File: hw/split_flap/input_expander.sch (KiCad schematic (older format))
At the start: 17 parts, among them J1 Conn_01x02, J2 Conn_01x02, J3 Conn_01x02, J4 Conn_01x02, J5 Conn_01x02, J6 Conn_01x02, J7 Conn_01x02, J8 Conn_01x02, U4 PCF8574

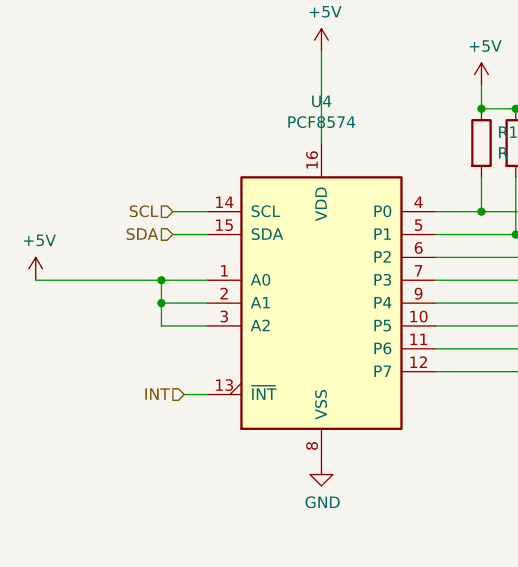
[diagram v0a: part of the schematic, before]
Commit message: Rework PCB
Start routing all expanders
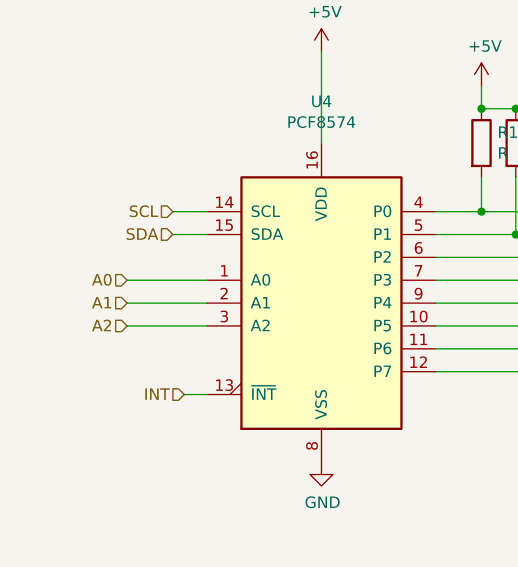
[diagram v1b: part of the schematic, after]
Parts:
- R1, R2, R3, R4, R5, R6, R7, R8: footprint Resistor_THT:R_Axial_DIN0207_L6.3mm_D2.5mm_P10.16mm_Horizontal -> Resistor_SMD:R_0805_2012Metric_Pad1.15x1.40mm_HandSolder
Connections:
- net +5V: no longer U4.1 (A0), U4.2 (A1), U4.3 (A2)
- new net A0: U4.1 (A0)
- new net A1: U4.2 (A1)
- new net A2: U4.3 (A2)
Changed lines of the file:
@@
 $Descr A4 11693 8268
 encoding utf-8
-Sheet 4 6
+Sheet 3 6
 Title ""
 Date ""
@@
 	4700 3100 4700 2700
 Wire Wire Line
-	4000 3700 4000 3800
-Wire Wire Line
-	4000 3700 4200 3700
-Wire Wire Line
-	4000 3800 4200 3800
-Wire Wire Line
 	4050 3400 4200 3400
 Wire Wire Line
 	4200 3500 4050 3500
-Wire Wire Line
-	4200 3900 4000 3900
 $Comp
 L power:GND #PWR?
@@
 F 0 "R2" H 5620 3146 50  0000 L CNN
 F 1 "R" H 5620 3055 50  0000 L CNN
-F 2 "Resistor_THT:R_Axial_DIN0207_L6.3mm_D2.5mm_P10.16mm_Horizontal" V 5480 3100 50  0001 C CNN
+F 2 "Resistor_SMD:R_0805_2012Metric_Pad1.15x1.40mm_HandSolder" V 5480 3100 50  0001 C CNN
 F 3 "~" H 5550 3100 50  0001 C CNN
 	1    5550 3100
@@
 F 0 "R3" H 5770 3146 50  0000 L CNN
 F 1 "R" H 5770 3055 50  0000 L CNN
-F 2 "Resistor_THT:R_Axial_DIN0207_L6.3mm_D2.5mm_P10.16mm_Horizontal" V 5630 3100 50  0001 C CNN
+F 2 "Resistor_SMD:R_0805_2012Metric_Pad1.15x1.40mm_HandSolder" V 5630 3100 50  0001 C CNN
 F 3 "~" H 5700 3100 50  0001 C CNN
 	1    5700 3100
@@
 F 0 "R4" H 5920 3146 50  0000 L CNN
 F 1 "R" H 5920 3055 50  0000 L CNN
-F 2 "Resistor_THT:R_Axial_DIN0207_L6.3mm_D2.5mm_P10.16mm_Horizontal" V 5780 3100 50  0001 C CNN
+F 2 "Resistor_SMD:R_0805_2012Metric_Pad1.15x1.40mm_HandSolder" V 5780 3100 50  0001 C CNN
 F 3 "~" H 5850 3100 50  0001 C CNN
 	1    5850 3100
@@
 F 0 "R5" H 6070 3146 50  0000 L CNN
 F 1 "R" H 6070 3055 50  0000 L CNN
-F 2 "Resistor_THT:R_Axial_DIN0207_L6.3mm_D2.5mm_P10.16mm_Horizontal" V 5930 3100 50  0001 C CNN
+F 2 "Resistor_SMD:R_0805_2012Metric_Pad1.15x1.40mm_HandSolder" V 5930 3100 50  0001 C CNN
 F 3 "~" H 6000 3100 50  0001 C CNN
 	1    6000 3100
@@
 F 0 "R6" H 6220 3146 50  0000 L CNN
 F 1 "R" H 6220 3055 50  0000 L CNN
-F 2 "Resistor_THT:R_Axial_DIN0207_L6.3mm_D2.5mm_P10.16mm_Horizontal" V 6080 3100 50  0001 C CNN
+F 2 "Resistor_SMD:R_0805_2012Metric_Pad1.15x1.40mm_HandSolder" V 6080 3100 50  0001 C CNN
 F 3 "~" H 6150 3100 50  0001 C CNN
 	1    6150 3100
@@
 F 0 "R7" H 6370 3146 50  0000 L CNN
 F 1 "R" H 6370 3055 50  0000 L CNN
-F 2 "Resistor_THT:R_Axial_DIN0207_L6.3mm_D2.5mm_P10.16mm_Horizontal" V 6230 3100 50  0001 C CNN
+F 2 "Resistor_SMD:R_0805_2012Metric_Pad1.15x1.40mm_HandSolder" V 6230 3100 50  0001 C CNN
 F 3 "~" H 6300 3100 50  0001 C CNN
 	1    6300 3100
@@
 F 0 "R1" H 5470 3146 50  0000 L CNN
 F 1 "R" H 5470 3055 50  0000 L CNN
-F 2 "Resistor_THT:R_Axial_DIN0207_L6.3mm_D2.5mm_P10.16mm_Horizontal" V 5330 3100 50  0001 C CNN
+F 2 "Resistor_SMD:R_0805_2012Metric_Pad1.15x1.40mm_HandSolder" V 5330 3100 50  0001 C CNN
 F 3 "~" H 5400 3100 50  0001 C CNN
 	1    5400 3100
@@
 F 0 "R8" H 6520 3146 50  0000 L CNN
 F 1 "R" H 6520 3055 50  0000 L CNN
-F 2 "Resistor_THT:R_Axial_DIN0207_L6.3mm_D2.5mm_P10.16mm_Horizontal" V 6380 3100 50  0001 C CNN
+F 2 "Resistor_SMD:R_0805_2012Metric_Pad1.15x1.40mm_HandSolder" V 6380 3100 50  0001 C CNN
 F 3 "~" H 6450 3100 50  0001 C CNN
 	1    6450 3100
@@
 	6450 4100 6750 4100
 Wire Wire Line
-	4000 3800 4000 3900
-Connection ~ 4000 3800
-Connection ~ 4000 3700
-Wire Wire Line
 	4100 4200 4200 4200
-$Comp
-L power:+5V #PWR?
-U 1 1 5E06FDAF
-P 3450 3700
-AR Path="/5E06FDAF" Ref="#PWR?"  Part="1"
-AR Path="/5E065378/5E06FDAF" Ref="#PWR014"  Part="1"
-F 0 "#PWR014" H 3450 3550 50  0001 C CNN
-F 1 "+5V" H 3465 3873 50  0000 C CNN
-F 2 "" H 3450 3700 50  0001 C CNN
-F 3 "" H 3450 3700 50  0001 C CNN
-	1    3450 3700
-	1    0    0    -1
-$EndComp
 $Comp
 L power:+5V #PWR?
@@
 Text HLabel 4050 3400 0    50   Input ~ 0
 SCL
-Wire Wire Line
-	3450 3700 4000 3700
 Text HLabel 4050 3500 0    50   Input ~ 0
 SDA
 Text HLabel 4100 4200 0    50   Input ~ 0
 INT
+Text HLabel 3850 3700 0    50   Input ~ 0
+A0
+Text HLabel 3850 3800 0    50   Input ~ 0
+A1
+Text HLabel 3850 3900 0    50   Input ~ 0
+A2
+Wire Wire Line
+	3850 3900 4200 3900
+Wire Wire Line
+	3850 3800 4200 3800
+Wire Wire Line
+	3850 3700 4200 3700
 $EndSCHEMATC

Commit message: Add VCC for motors
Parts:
- J1, J2, J3, J4, J5, J6, J7, J8: footprint Connector_JST:JST_XH_B2B-XH-A_1x02_P2.50mm_Vertical -> Connector_JST:JST_XH_B3B-XH-A_1x03_P2.50mm_Vertical; symbol Connector_Generic:Conn_01x02 -> Connector_Generic:Conn_01x03
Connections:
- net +5V: now also J1.2 (Pin_2), J2.2 (Pin_2), J3.2 (Pin_2), J4.2 (Pin_2), J5.2 (Pin_2), J6.2 (Pin_2), J7.2 (Pin_2), J8.2 (Pin_2)
- net GND: now also J1.3 (Pin_3), J2.3 (Pin_3), J3.3 (Pin_3), J4.3 (Pin_3), J5.3 (Pin_3), J6.3 (Pin_3), J7.3 (Pin_3), J8.3 (Pin_3); no longer J1.2 (Pin_2), J2.2 (Pin_2), J3.2 (Pin_2), J4.2 (Pin_2), J5.2 (Pin_2), J6.2 (Pin_2), J7.2 (Pin_2), J8.2 (Pin_2)
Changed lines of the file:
@@
 $EndComp
-Wire Wire Line
-	6750 4950 7050 4950
-Wire Wire Line
-	6750 4100 6750 4950
 Wire Wire Line
 	5200 4100 6450 4100
-Wire Wire Line
-	6800 4550 7050 4550
-Wire Wire Line
-	6800 4000 6800 4550
-Wire Wire Line
-	6850 4150 7050 4150
-Wire Wire Line
-	6850 3900 6850 4150
-Wire Wire Line
-	6900 3750 7050 3750
-Wire Wire Line
-	6900 3800 6900 3750
-Wire Wire Line
-	6850 3350 7050 3350
-Wire Wire Line
-	6850 3700 6850 3350
-Wire Wire Line
-	6800 2950 7050 2950
-Wire Wire Line
-	6800 3600 6800 2950
-Wire Wire Line
-	6750 2550 7050 2550
-Wire Wire Line
-	6750 3500 6750 2550
-Wire Wire Line
-	6700 2150 7050 2150
-Wire Wire Line
-	6700 3400 6700 2150
 $Comp
 L power:GND #PWR?
@@
 $EndComp
 $Comp
-L Connector_Generic:Conn_01x02 J?
-U 1 1 5E06FCF0
-P 7250 2150
-AR Path="/5E06FCF0" Ref="J?"  Part="1"
-AR Path="/5E065378/5E06FCF0" Ref="J1"  Part="1"
-F 0 "J1" H 7330 2142 50  0000 L CNN
-F 1 "Conn_01x02" H 7330 2051 50  0000 L CNN
-F 2 "Connector_JST:JST_XH_B2B-XH-A_1x02_P2.50mm_Vertical" H 7250 2150 50  0001 C CNN
-F 3 "~" H 7250 2150 50  0001 C CNN
-	1    7250 2150
-	1    0    0    -1
-$EndComp
-$Comp
 L power:GND #PWR?
 U 1 1 5E06FCF6
@@
 $EndComp
 $Comp
-L Connector_Generic:Conn_01x02 J?
+L Connector_Generic:Conn_01x03 J?
 U 1 1 5E06FCFC
 P 7250 2550
@@
 F 0 "J2" H 7330 2542 50  0000 L CNN
 F 1 "Conn_01x02" H 7330 2451 50  0000 L CNN
-F 2 "Connector_JST:JST_XH_B2B-XH-A_1x02_P2.50mm_Vertical" H 7250 2550 50  0001 C CNN
+F 2 "Connector_JST:JST_XH_B3B-XH-A_1x03_P2.50mm_Vertical" H 7250 2550 50  0001 C CNN
 F 3 "~" H 7250 2550 50  0001 C CNN
 	1    7250 2550
@@
 $EndComp
 $Comp
-L Connector_Generic:Conn_01x02 J?
+L Connector_Generic:Conn_01x03 J?
 U 1 1 5E06FD08
 P 7250 2950
@@
 F 0 "J3" H 7330 2942 50  0000 L CNN
 F 1 "Conn_01x02" H 7330 2851 50  0000 L CNN
-F 2 "Connector_JST:JST_XH_B2B-XH-A_1x02_P2.50mm_Vertical" H 7250 2950 50  0001 C CNN
+F 2 "Connector_JST:JST_XH_B3B-XH-A_1x03_P2.50mm_Vertical" H 7250 2950 50  0001 C CNN
 F 3 "~" H 7250 2950 50  0001 C CNN
 	1    7250 2950
@@
 $EndComp
 $Comp
-L Connector_Generic:Conn_01x02 J?
+L Connector_Generic:Conn_01x03 J?
 U 1 1 5E06FD14
 P 7250 3350
@@
 F 0 "J4" H 7330 3342 50  0000 L CNN
 F 1 "Conn_01x02" H 7330 3251 50  0000 L CNN
-F 2 "Connector_JST:JST_XH_B2B-XH-A_1x02_P2.50mm_Vertical" H 7250 3350 50  0001 C CNN
+F 2 "Connector_JST:JST_XH_B3B-XH-A_1x03_P2.50mm_Vertical" H 7250 3350 50  0001 C CNN
 F 3 "~" H 7250 3350 50  0001 C CNN
 	1    7250 3350
@@
 $EndComp
 $Comp
-L Connector_Generic:Conn_01x02 J?
+L Connector_Generic:Conn_01x03 J?
 U 1 1 5E06FD20
 P 7250 3750
@@
 F 0 "J5" H 7330 3742 50  0000 L CNN
 F 1 "Conn_01x02" H 7330 3651 50  0000 L CNN
-F 2 "Connector_JST:JST_XH_B2B-XH-A_1x02_P2.50mm_Vertical" H 7250 3750 50  0001 C CNN
+F 2 "Connector_JST:JST_XH_B3B-XH-A_1x03_P2.50mm_Vertical" H 7250 3750 50  0001 C CNN
 F 3 "~" H 7250 3750 50  0001 C CNN
 	1    7250 3750
@@
 $EndComp
 $Comp
-L Connector_Generic:Conn_01x02 J?
+L Connector_Generic:Conn_01x03 J?
 U 1 1 5E06FD2C
 P 7250 4150
@@
 F 0 "J6" H 7330 4142 50  0000 L CNN
 F 1 "Conn_01x02" H 7330 4051 50  0000 L CNN
-F 2 "Connector_JST:JST_XH_B2B-XH-A_1x02_P2.50mm_Vertical" H 7250 4150 50  0001 C CNN
+F 2 "Connector_JST:JST_XH_B3B-XH-A_1x03_P2.50mm_Vertical" H 7250 4150 50  0001 C CNN
 F 3 "~" H 7250 4150 50  0001 C CNN
 	1    7250 4150
@@
 $EndComp
 $Comp
-L Connector_Generic:Conn_01x02 J?
+L Connector_Generic:Conn_01x03 J?
 U 1 1 5E06FD3E
 P 7250 4950
@@
 F 0 "J8" H 7330 4942 50  0000 L CNN
 F 1 "Conn_01x02" H 7330 4851 50  0000 L CNN
-F 2 "Connector_JST:JST_XH_B2B-XH-A_1x02_P2.50mm_Vertical" H 7250 4950 50  0001 C CNN
+F 2 "Connector_JST:JST_XH_B3B-XH-A_1x03_P2.50mm_Vertical" H 7250 4950 50  0001 C CNN
 F 3 "~" H 7250 4950 50  0001 C CNN
 	1    7250 4950
@@
 $EndComp
 $Comp
-L Connector_Generic:Conn_01x02 J?
+L Connector_Generic:Conn_01x03 J?
 U 1 1 5E06FD44
 P 7250 4550
@@
 F 0 "J7" H 7330 4542 50  0000 L CNN
 F 1 "Conn_01x02" H 7330 4451 50  0000 L CNN
-F 2 "Connector_JST:JST_XH_B2B-XH-A_1x02_P2.50mm_Vertical" H 7250 4550 50  0001 C CNN
+F 2 "Connector_JST:JST_XH_B3B-XH-A_1x03_P2.50mm_Vertical" H 7250 4550 50  0001 C CNN
 F 3 "~" H 7250 4550 50  0001 C CNN
 	1    7250 4550
@@
 Wire Wire Line
 	3850 3700 4200 3700
+$Comp
+L Connector_Generic:Conn_01x03 J?
+U 1 1 5E06FCF0
+P 7250 2150
+AR Path="/5E06FCF0" Ref="J?"  Part="1"
+AR Path="/5E065378/5E06FCF0" Ref="J1"  Part="1"
+F 0 "J1" H 7330 2142 50  0000 L CNN
+F 1 "Conn_01x02" H 7330 2051 50  0000 L CNN
+F 2 "Connector_JST:JST_XH_B3B-XH-A_1x03_P2.50mm_Vertical" H 7250 2150 50  0001 C CNN
+F 3 "~" H 7250 2150 50  0001 C CNN
+	1    7250 2150
+	1    0    0    -1
+$EndComp
+Wire Wire Line
+	6700 2050 7050 2050
+Wire Wire Line
+	6700 2050 6700 3400
+Wire Wire Line
+	6750 2450 7050 2450
+Wire Wire Line
+	6750 2450 6750 3500
+Wire Wire Line
+	6800 2850 7050 2850
+Wire Wire Line
+	6800 2850 6800 3600
+Wire Wire Line
+	6850 3250 7050 3250
+Wire Wire Line
+	6850 3250 6850 3700
+Wire Wire Line
+	6900 3650 7050 3650
+Wire Wire Line
+	6900 3650 6900 3800
+Wire Wire Line
+	6850 3900 6850 4050
+Wire Wire Line
+	6850 4050 7050 4050
+Wire Wire Line
+	6800 4000 6800 4450
+Wire Wire Line
+	6800 4450 7050 4450
+Wire Wire Line
+	6750 4100 6750 4850
+Wire Wire Line
+	6750 4850 7050 4850
+$Comp
+L power:+5V #PWR062
+U 1 1 5DFB10BE
+P 6900 4150
+F 0 "#PWR062" H 6900 4000 50  0001 C CNN
+F 1 "+5V" H 6915 4323 50  0000 C CNN
+F 2 "" H 6900 4150 50  0001 C CNN
+F 3 "" H 6900 4150 50  0001 C CNN
+	1    6900 4150
+	1    0    0    -1
+$EndComp
+$Comp
+L power:+5V #PWR063
+U 1 1 5DFB1594
+P 6900 4550
+F 0 "#PWR063" H 6900 4400 50  0001 C CNN
+F 1 "+5V" H 6915 4723 50  0000 C CNN
+F 2 "" H 6900 4550 50  0001 C CNN
+F 3 "" H 6900 4550 50  0001 C CNN
+	1    6900 4550
+	1    0    0    -1
+$EndComp
+$Comp
+L power:+5V #PWR064
+U 1 1 5DFB1958
+P 6900 4950
+F 0 "#PWR064" H 6900 4800 50  0001 C CNN
+F 1 "+5V" H 6915 5123 50  0000 C CNN
+F 2 "" H 6900 4950 50  0001 C CNN
+F 3 "" H 6900 4950 50  0001 C CNN
+	1    6900 4950
+	1    0    0    -1
+$EndComp
+$Comp
+L power:+5V #PWR067
+U 1 1 5DFB236A
+P 6950 3750
+F 0 "#PWR067" H 6950 3600 50  0001 C CNN
+F 1 "+5V" H 6965 3923 50  0000 C CNN
+F 2 "" H 6950 3750 50  0001 C CNN
+F 3 "" H 6950 3750 50  0001 C CNN
+	1    6950 3750
+	1    0    0    -1
+$EndComp
+$Comp
+L power:+5V #PWR066
+U 1 1 5DFB2680
+P 6950 3350
+F 0 "#PWR066" H 6950 3200 50  0001 C CNN
+F 1 "+5V" H 6965 3523 50  0000 C CNN
+F 2 "" H 6950 3350 50  0001 C CNN
+F 3 "" H 6950 3350 50  0001 C CNN
+	1    6950 3350
+	1    0    0    -1
+$EndComp
+$Comp
+L power:+5V #PWR065
+U 1 1 5DFB3078
+P 6950 2950
+F 0 "#PWR065" H 6950 2800 50  0001 C CNN
+F 1 "+5V" H 6965 3123 50  0000 C CNN
+F 2 "" H 6950 2950 50  0001 C CNN
+F 3 "" H 6950 2950 50  0001 C CNN
+	1    6950 2950
+	1    0    0    -1
+$EndComp
+$Comp
+L power:+5V #PWR061
+U 1 1 5DFB33BC
+P 6900 2550
+F 0 "#PWR061" H 6900 2400 50  0001 C CNN
+F 1 "+5V" H 6915 2723 50  0000 C CNN
+F 2 "" H 6900 2550 50  0001 C CNN
+F 3 "" H 6900 2550 50  0001 C CNN
+	1    6900 2550
+	1    0    0    -1
+$EndComp
+$Comp
+L power:+5V #PWR060
+U 1 1 5DFB3F11
+P 6900 2150
+F 0 "#PWR060" H 6900 2000 50  0001 C CNN
+F 1 "+5V" H 6915 2323 50  0000 C CNN
+F 2 "" H 6900 2150 50  0001 C CNN
+F 3 "" H 6900 2150 50  0001 C CNN
+	1    6900 2150
+	1    0    0    -1
+$EndComp
+Wire Wire Line
+	7050 2150 6900 2150
+Wire Wire Line
+	6900 2550 7050 2550
+Wire Wire Line
+	6950 2950 7050 2950
+Wire Wire Line
+	6950 3350 7050 3350
+Wire Wire Line
+	6950 3750 7050 3750
+Wire Wire Line
+	6900 4150 7050 4150
+Wire Wire Line
+	6900 4550 7050 4550
+Wire Wire Line
+	6900 4950 7050 4950
 $EndSCHEMATC
